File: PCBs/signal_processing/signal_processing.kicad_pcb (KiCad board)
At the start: 2 copper layers, 75 x 36 mm, 140 parts, among them IC1 AD8066, IC2 ADG701BRTZN, IC3 AD8066, IC4 AD8066, IC5 LT1713, IC6 LT1713, IC7 AD8066, X1 87437-0443, X2 87437-0443, X3 87437-0443

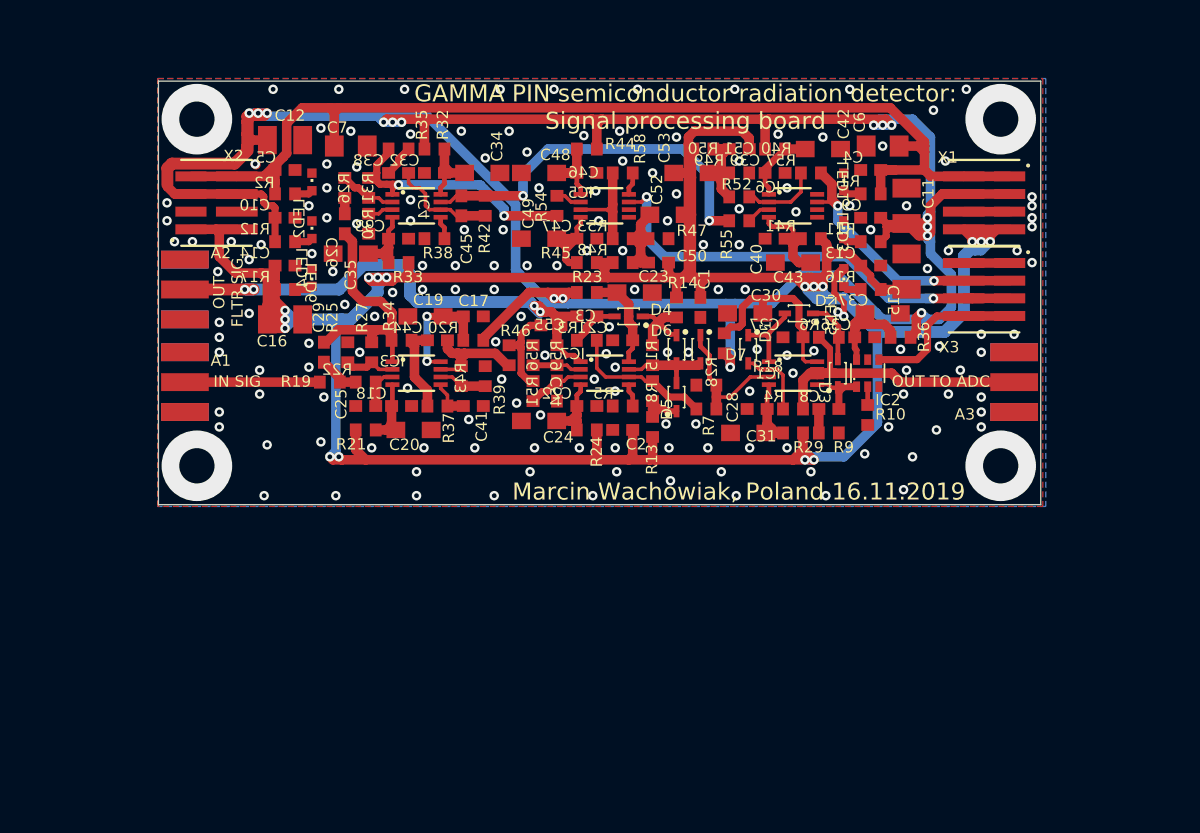
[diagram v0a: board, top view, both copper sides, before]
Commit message: Reorganization of pcb files
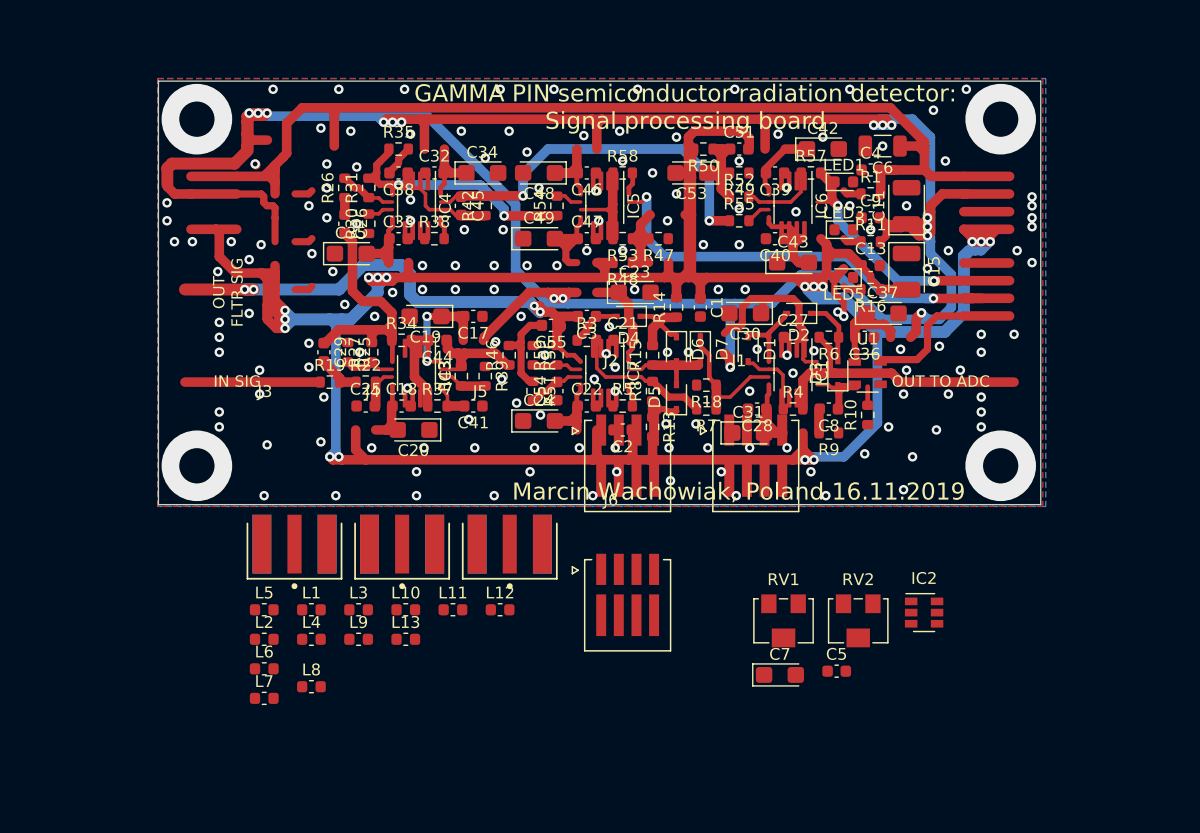
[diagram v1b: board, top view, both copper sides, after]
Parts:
- removed A1, A2, A3: SMA-EDGE-0.062, signal_processing:CONSMA003.062
- removed C10, C14, C50: 100n/50V, signal_processing:C0603
- removed C12, C16: 47u/6V, signal_processing:SMC_B
- removed C52: 4,7u/6V, signal_processing:SMC_A
- removed LED2, LED4, LED6: GREEN, signal_processing:CHIPLED_0603
- removed R12, R17: 300, signal_processing:R0603
- removed R2: 43k, signal_processing:R0603
- removed R20, R21, R23, R24, R28, R29, R32, R33, R36, R40, R41, R44, R45: 1, signal_processing:R0603
- removed X1, X2, X3: 87437-0443, signal_processing:87437-0443
- added IC2: ADG701BRTZN, Package_TO_SOT_SMD:SOT-23-6, F.Cu at (176.1, 132.2)
- added J1: 874380443, semiconductor_radiation_detector:87438-0443, F.Cu at (161.8, 119.7)
- added J2: 874380443, semiconductor_radiation_detector:87438-0443, F.Cu at (150.9, 119.7)
- added J3: CON-SMA-EDGE-S, semiconductor_radiation_detector:CON-SMA-EDGE-S, F.Cu at (122.6, 119.1)
- added J4: CON-SMA-EDGE-S, semiconductor_radiation_detector:CON-SMA-EDGE-S, F.Cu at (131.7, 119.1)
- added J5: CON-SMA-EDGE-S, semiconductor_radiation_detector:CON-SMA-EDGE-S, F.Cu at (140.9, 119.1)
- added J6: 874380443, semiconductor_radiation_detector:87438-0443, F.Cu at (150.9, 131.6)
- added L1: 1u, Inductor_SMD:L_0603_1608Metric, F.Cu at (124.0, 131.9)
- added L10: 1u, Inductor_SMD:L_0603_1608Metric, F.Cu at (132.0, 131.9)
- added L11: 1u, Inductor_SMD:L_0603_1608Metric, F.Cu at (136.0, 131.9)
- added L12: 1u, Inductor_SMD:L_0603_1608Metric, F.Cu at (140.0, 131.9)
- added L13: 1u, Inductor_SMD:L_0603_1608Metric, F.Cu at (132.0, 134.5)
- added L2: 1u, Inductor_SMD:L_0603_1608Metric, F.Cu at (120.0, 134.5)
- added L3: 1u, Inductor_SMD:L_0603_1608Metric, F.Cu at (128.0, 131.9)
- added L4: 1u, Inductor_SMD:L_0603_1608Metric, F.Cu at (124.0, 134.5)
- added L5: 1u, Inductor_SMD:L_0603_1608Metric, F.Cu at (120.0, 131.9)
- added L6: 1u, Inductor_SMD:L_0603_1608Metric, F.Cu at (120.0, 137.0)
- added L7: 1u, Inductor_SMD:L_0603_1608Metric, F.Cu at (120.0, 139.5)
- added L8: 1u, Inductor_SMD:L_0603_1608Metric, F.Cu at (124.0, 138.5)
- added L9: 1u, Inductor_SMD:L_0603_1608Metric, F.Cu at (128.0, 134.5)
- added RV1: 500, Potentiometer_SMD:Potentiometer_Bourns_3224W_Vertical, F.Cu at (164.1, 132.9)
- added RV2: 10, Potentiometer_SMD:Potentiometer_Bourns_3224W_Vertical, F.Cu at (170.5, 132.9)
- C1, C13, C17, C18, C2, C21, C22, C25, C26, C27, C28, C29, C3, C32, C33, C36, C38, C39, C4, C40, C41, C44, C45, C46, C47, C51, C54, C55, C8, C9: footprint signal_processing:C0603 -> Capacitor_SMD:C_0603_1608Metric
- C11, C15: footprint signal_processing:SMC_B -> Capacitor_Tantalum_SMD:CP_EIA-3528-21_Kemet-B
- C19, C20, C23, C24, C30, C31, C34, C35, C37, C42, C43, C48, C49, C53: footprint signal_processing:SMC_A -> Capacitor_Tantalum_SMD:CP_EIA-3216-18_Kemet-A
- C5: value 1n/100V -> 100n/50V; footprint signal_processing:C0603 -> Capacitor_SMD:C_0603_1608Metric
- C6: footprint signal_processing:C1206 -> Capacitor_SMD:C_1206_3216Metric
- C7: value 4,7u/50V -> 4,7u/6V; footprint signal_processing:C1206 -> Capacitor_Tantalum_SMD:CP_EIA-3216-18_Kemet-A
- D1, D2, D3, D4, D5, D6, D7: footprint signal_processing:SOD2514X100N -> Diode_SMD:D_SOD-323
- IC1, IC3, IC4, IC5, IC6, IC7: footprint signal_processing:MSOP8 -> Package_SO:MSOP-8_3x3mm_P0.65mm
- LED1, LED3, LED5: footprint signal_processing:CHIPLED_0603 -> LED_SMD:LED_0603_1608Metric
- R1, R10, R11, R13, R14, R15, R16, R18, R19, R22, R25, R26, R27, R3, R30, R31, R34, R35, R37, R38, R39, R4, R42, R43, R46, R47, R48, R49, R5, R50, R51, R52, R53, R54, R55, R56, R57, R58, R59, R6, R7, R8, R9: footprint signal_processing:R0603 -> Resistor_SMD:R_0603_1608Metric
- U1: renamed from IC2; value ADG701BRTZN -> ADG701; footprint signal_processing:SOT23-6 -> Package_TO_SOT_SMD:SOT-23-6
- moved C5 63.4 mm to (168.7, 137.2), turned to 0 degrees
- moved C7 57.9 mm to (163.8, 137.5)
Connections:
- C5 pad 1: GND -> Net-(C5-Pad1)
- C5 pad 2: /+65V -> -5V
- C7 pad 1: /+65V -> Net-(C5-Pad1)
- C7 pad 2: GND -> -5V
- IC1 pad 1: Net-(D1-PadK) -> Net-(D1-Pad1)
- IC1 pad 2: Net-(D1-PadA) -> Net-(D1-Pad2)
- IC6 pad 7: /RISING_SLOPE -> Net-(IC6-Pad7)
- IC6 pad 8: (no net) -> /RISING_SLOPE
- IC7 pad 7: Net-(D5-PadA) -> Net-(D5-Pad2)
- R1 pad 1: Net-(LED1-PadA) -> /+65V
- R1 pad 2: /+65V -> Net-(LED1-Pad2)
- R10 pad 1: GND -> Net-(R10-Pad1)
- R10 pad 2: Net-(IC2-Pad2) -> GND
- R11 pad 1: Net-(LED3-PadA) -> +5V
- R11 pad 2: +5V -> Net-(LED3-Pad2)
- R13 pad 1: Net-(D5-PadK) -> -5V
- R13 pad 2: -5V -> Net-(D5-Pad1)
- R14 pad 1: Net-(D4-PadK) -> -5V
- R14 pad 2: -5V -> Net-(D4-Pad1)
- R15 pad 1: Net-(D5-PadA) -> Net-(D4-Pad1)
- R15 pad 2: Net-(D4-PadK) -> Net-(D5-Pad2)
- R16 pad 1: -5V -> Net-(LED5-Pad1)
- R16 pad 2: Net-(LED5-PadC) -> -5V
- R18 pad 1: /BLR_OUT -> GND
- R18 pad 2: GND -> /BLR_OUT
- R19 pad 1: /SIGNAL_INPUT -> Net-(C29-Pad2)
- R19 pad 2: Net-(C29-Pad2) -> /SIGNAL_INPUT
- R22 pad 1: Net-(C29-Pad2) -> Net-(C25-Pad2)
- R22 pad 2: Net-(C25-Pad2) -> Net-(C29-Pad2)
- R25 pad 1: GND -> Net-(IC3-Pad2)
- R25 pad 2: Net-(IC3-Pad2) -> GND
- R27 pad 1: Net-(IC3-Pad2) -> /FAST_FILTERED_SIG
- R27 pad 2: /FAST_FILTERED_SIG -> Net-(IC3-Pad2)
- R3 pad 1: Net-(C3-Pad1) -> Net-(IC7-Pad6)
- R3 pad 2: Net-(IC7-Pad6) -> Net-(C3-Pad1)
- R30 pad 1: GND -> Net-(IC4-Pad3)
- R30 pad 2: Net-(IC4-Pad3) -> GND
- R31 pad 1: Net-(IC4-Pad2) -> Net-(IC4-Pad1)
- R31 pad 2: Net-(IC4-Pad1) -> Net-(IC4-Pad2)
- R34 pad 1: /FAST_FILTERED_SIG -> Net-(C44-Pad2)
- R34 pad 2: Net-(C44-Pad2) -> /FAST_FILTERED_SIG
- R35 pad 1: Net-(IC4-Pad1) -> Net-(C38-Pad2)
- R35 pad 2: Net-(C38-Pad2) -> Net-(IC4-Pad1)
- R37 pad 1: Net-(C44-Pad2) -> Net-(C41-Pad2)
- R37 pad 2: Net-(C41-Pad2) -> Net-(C44-Pad2)
- R38 pad 1: GND -> Net-(IC4-Pad5)
- R38 pad 2: Net-(IC4-Pad5) -> GND
- R39 pad 1: GND -> Net-(IC3-Pad6)
- R39 pad 2: Net-(IC3-Pad6) -> GND
- R4 pad 1: Net-(D1-PadA) -> /ADC
- R4 pad 2: /ADC -> Net-(D1-Pad2)
- R42 pad 1: Net-(C38-Pad1) -> Net-(C45-Pad1)
- R42 pad 2: Net-(C45-Pad1) -> Net-(C38-Pad1)
- R43 pad 1: Net-(IC3-Pad6) -> Net-(C44-Pad1)
- R43 pad 2: Net-(C44-Pad1) -> Net-(IC3-Pad6)
- R46 pad 1: Net-(C44-Pad1) -> Net-(C55-Pad2)
- R46 pad 2: Net-(C55-Pad2) -> Net-(C44-Pad1)
- R47 pad 1: GND -> Net-(R47-Pad1)
- R47 pad 2: Net-(C50-Pad1) -> GND
- R48 pad 1: Net-(C50-Pad1) -> -5V
- R48 pad 2: -5V -> Net-(R48-Pad2)
- R49 pad 1: GND -> Net-(R49-Pad1)
- R49 pad 2: Net-(C51-Pad1) -> GND
- R5 pad 1: GND -> Net-(IC7-Pad5)
- R5 pad 2: Net-(IC7-Pad5) -> GND
- R50 pad 1: Net-(C51-Pad1) -> -5V
- R50 pad 2: -5V -> Net-(R50-Pad2)
- R51 pad 1: Net-(C55-Pad2) -> Net-(C54-Pad2)
- R51 pad 2: Net-(C54-Pad2) -> Net-(C55-Pad2)
- R52 pad 1: Net-(C51-Pad1) -> Net-(IC6-Pad2)
- R52 pad 2: Net-(IC6-Pad2) -> Net-(C51-Pad1)
- R53 pad 1: Net-(C50-Pad1) -> Net-(IC5-Pad3)
- R53 pad 2: Net-(IC5-Pad3) -> Net-(C5-Pad1)
- R54 pad 1: Net-(IC4-Pad1) -> Net-(IC5-Pad2)
- R54 pad 2: Net-(IC5-Pad2) -> Net-(IC4-Pad1)
- R55 pad 1: Net-(C45-Pad1) -> Net-(IC6-Pad3)
- R55 pad 2: Net-(IC6-Pad3) -> Net-(C45-Pad1)
- R56 pad 1: GND -> Net-(IC7-Pad2)
- R56 pad 2: Net-(IC7-Pad2) -> GND
- R57 pad 1: Net-(IC6-Pad2) -> Net-(IC6-Pad7)
- R57 pad 2: /RISING_SLOPE -> Net-(IC6-Pad2)
- R58 pad 1: Net-(IC5-Pad3) -> Net-(IC5-Pad8)
- R58 pad 2: Net-(IC5-Pad8) -> Net-(IC5-Pad3)
- R59 pad 1: Net-(IC7-Pad2) -> /FILTERED_SIGNAL
- R59 pad 2: /FILTERED_SIGNAL -> Net-(IC7-Pad2)
- R6 pad 1: Net-(D2-PadK) -> /ADC
- R6 pad 2: /ADC -> Net-(D2-Pad1)
- R7 pad 1: /BLR_OUT -> Net-(IC7-Pad6)
- R7 pad 2: Net-(IC7-Pad6) -> /BLR_OUT
- R8 pad 1: Net-(D5-PadK) -> Net-(IC7-Pad6)
- R8 pad 2: Net-(IC7-Pad6) -> Net-(D5-Pad1)
- R9 pad 1: GND -> Net-(C8-Pad2)
- R9 pad 2: Net-(C8-Pad2) -> GND
- U1 pad 2: Net-(IC2-Pad2) -> Net-(R10-Pad1)
- U1 pad 3: GND -> (no net)
- U1 pad 6: Net-(C36-Pad2) -> (no net)
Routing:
- net /RESET: track 13.8 -> 0.00 mm
- net (no net): track 0.00 -> 13.8 mm
- net Net-(C29-Pad2): track 3.93 -> 15.4 mm
- net /SIGNAL_INPUT: track 11.5 -> 0.00 mm
- net GND: track 12.7 -> 20.4 mm, vias 167 -> 162
- net Net-(D1-PadK): track 6.76 -> 0.00 mm
- net Net-(D1-Pad1): track 0.00 -> 6.76 mm
- net Net-(IC4-Pad1): track 24.2 -> 26.4 mm
- net Net-(IC5-Pad2): track 2.23 -> 0.00 mm
- net Net-(IC4-Pad3): track 2.16 -> 0.00 mm
- net Net-(IC6-Pad3): track 2.06 -> 0.00 mm, vias 0 -> 1
- net Net-(C45-Pad1): track 32.2 -> 34.3 mm
- net Net-(IC5-Pad3): track 9.03 -> 11.0 mm
- net Net-(IC7-Pad5): track 1.95 -> 0.00 mm
- net Net-(IC5-Pad8): track 1.95 -> 0.00 mm
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
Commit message: finished preamplifier board redesigning
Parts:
- removed the IC1 at (164.9, 111.8)
- removed the IC7 at (148.9, 111.8)
- added IC2: AD8066, Package_SO:MSOP-8_3x3mm_P0.65mm, F.Cu at (140.1, 141.9)
- added IC3: AD8066, Package_SO:MSOP-8_3x3mm_P0.65mm, F.Cu at (140.1, 146.4)
- added R44: 1k, Resistor_SMD:R_0603_1608Metric, F.Cu at (153.2, 140.8)
- added R45: 2k, Resistor_SMD:R_0603_1608Metric, F.Cu at (153.2, 143.3)
- added R46: 1k, Resistor_SMD:R_0603_1608Metric, F.Cu at (153.2, 145.9)
- added R47: 2k, Resistor_SMD:R_0603_1608Metric, F.Cu at (153.2, 148.4)
- IC5: renamed from IC2; value ADG701BRTZN -> ADG701
- moved IC6 51.8 mm to (147.5, 146.4), turned to 0 degrees
- moved J2 51.3 mm to (104.8, 97.2), turned to 270 degrees
- moved J6 48.5 mm to (191.5, 105.2), turned to 90 degrees
- moved IC4 46.6 mm to (147.5, 141.9), turned to 0 degrees
- moved J1 35.6 mm to (189.4, 97.3), turned to 90 degrees
- renumbered C15 to C10, C17 to C11, C18 to C12, C19 to C13, C20 to C14, C21 to C15, C22 to C16, C23 to C17, C24 to C18, C26 to C19, C25 to C20, C29 to C21, C27 to C22, C28 to C23, C30 to C24, C31 to C25, C32 to C26, C33 to C27, C34 to C28, C35 to C29, C36 to C30, C37 to C31, C38 to C32, C39 to C33, C40 to C34, C41 to C35, C42 to C36, C43 to C37, C44 to C38, C45 to C39, C46 to C40, C47 to C41, C48 to C42, C49 to C43, C51 to C44, C5 to C45, C53 to C46, C7 to C47, C54 to C48, C55 to C49, C6 to C5, C8 to C6, C9 to C7, C11 to C8, C13 to C9, IC3 to IC1, IC5 to IC7, LED3 to LED2, LED5 to LED3, R3 to R1, R13 to R10, R14 to R12, R15 to R13, R18 to R14, R16 to R15, R19 to R16, R22 to R17, R25 to R18, R26 to R19, R4 to R2, R27 to R20, R30 to R21, R31 to R22, R34 to R23, R35 to R24, R37 to R25, R38 to R26, R39 to R27, R42 to R28, R43 to R29, R5 to R3, R49 to R30, R50 to R31, R46 to R32, R47 to R33, R48 to R34, R51 to R35, R52 to R36, R55 to R37, R53 to R38, R54 to R39, R1 to R4, R56 to R40, R57 to R41, R58 to R42, R59 to R43, R6 to R5, R7 to R6, R8 to R7, R9 to R8, R10 to R9
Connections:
- C20 pad 2: Net-(C25-Pad2) -> Net-(C20-Pad2)
- C32 pad 1: Net-(C38-Pad1) -> Net-(C32-Pad1)
- C35 pad 2: Net-(C41-Pad2) -> Net-(C35-Pad2)
- C38 pad 1: Net-(C44-Pad1) (its old number) -> Net-(C38-Pad1)
- C39 pad 1: Net-(C45-Pad1) (its old number) -> Net-(C39-Pad1)
- C39 pad 2: Net-(C38-Pad1) -> Net-(C32-Pad1)
- C48 pad 2: Net-(C54-Pad2) -> Net-(C48-Pad2)
- IC1 pad 1: /FAST_FILTERED_SIG -> Net-(D1-Pad1)
- IC1 pad 2: Net-(IC3-Pad2) -> Net-(D1-Pad2)
- IC1 pad 3: Net-(C25-Pad2) -> /BLR_OUT
- IC1 pad 5: Net-(C41-Pad2) -> Net-(IC1-Pad5)
- IC1 pad 6: Net-(IC3-Pad6) -> Net-(IC1-Pad6)
- IC1 pad 7: Net-(C44-Pad1) (its old number) -> Net-(D5-Pad2)
- IC4 pad 1: Net-(IC4-Pad1) -> /FILTERED_SIGNAL
- IC4 pad 3: Net-(IC4-Pad3) -> Net-(C48-Pad2)
- IC4 pad 5: Net-(IC4-Pad5) -> Net-(C35-Pad2)
- IC4 pad 6: Net-(C38-Pad1) -> Net-(IC4-Pad6)
- IC4 pad 7: Net-(C45-Pad1) (its old number) -> Net-(C38-Pad1)
- IC6 pad 8: /RISING_SLOPE -> Net-(IC6-Pad8)
- IC7 pad 7: /PULSE_DURATION -> Net-(IC7-Pad7)
- R1 pad 1: Net-(IC7-Pad6) -> Net-(IC1-Pad6)
- R17 pad 1: Net-(C25-Pad2) -> Net-(C20-Pad2)
- R18 pad 1: Net-(IC3-Pad2) -> Net-(IC2-Pad2)
- R19 pad 2: Net-(IC4-Pad2) -> Net-(IC3-Pad2)
- R20 pad 2: Net-(IC3-Pad2) -> Net-(IC2-Pad2)
- R21 pad 1: Net-(IC4-Pad3) -> Net-(IC3-Pad3)
- R22 pad 1: Net-(IC4-Pad1) -> Net-(IC3-Pad1)
- R22 pad 2: Net-(IC4-Pad2) -> Net-(IC3-Pad2)
- R24 pad 2: Net-(IC4-Pad1) -> Net-(IC3-Pad1)
- R25 pad 1: Net-(C41-Pad2) -> Net-(C35-Pad2)
- R26 pad 1: Net-(IC4-Pad5) -> Net-(IC3-Pad5)
- R27 pad 1: Net-(IC3-Pad6) -> Net-(IC4-Pad6)
- R28 pad 1: Net-(C45-Pad1) (its old number) -> Net-(C39-Pad1)
- R28 pad 2: Net-(C38-Pad1) -> Net-(C32-Pad1)
- R29 pad 1: Net-(C44-Pad1) (its old number) -> Net-(C38-Pad1)
- R29 pad 2: Net-(IC3-Pad6) -> Net-(IC4-Pad6)
- R3 pad 1: Net-(IC7-Pad5) -> Net-(IC1-Pad5)
- R32 pad 2: Net-(C44-Pad1) (its old number) -> Net-(C38-Pad1)
- R35 pad 1: Net-(C54-Pad2) -> Net-(C48-Pad2)
- R37 pad 2: Net-(C45-Pad1) (its old number) -> Net-(C39-Pad1)
- R39 pad 2: Net-(IC4-Pad1) -> Net-(IC3-Pad1)
- R40 pad 1: Net-(IC7-Pad2) (its old number) -> Net-(IC4-Pad2)
- R43 pad 2: Net-(IC7-Pad2) (its old number) -> Net-(IC4-Pad2)
- R6 pad 1: Net-(IC7-Pad6) -> Net-(IC1-Pad6)
- R7 pad 1: Net-(IC7-Pad6) -> Net-(IC1-Pad6)
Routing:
- net Net-(C45-Pad1) (its old number): track 34.3 -> 0.00 mm, vias 2 -> 0
- net Net-(C45-Pad1): track 0.00 -> 32.2 mm, vias 0 -> 2
- net Net-(C44-Pad1) (its old number): track 11.3 -> 0.00 mm
- net Net-(C51-Pad1): track 0.00 -> 11.3 mm
- net Net-(IC7-Pad3): track 11.0 -> 1.95 mm
- net Net-(IC5-Pad3): track 0.00 -> 9.03 mm
- net Net-(C36-Pad2): track 0.00 -> 8.67 mm
- net Net-(C30-Pad2): track 8.67 -> 0.00 mm
- net Net-(C55-Pad2): track 0.00 -> 8.13 mm
- net Net-(C49-Pad2): track 8.13 -> 0.00 mm
- net Net-(C44-Pad2): track 0.00 -> 8.04 mm
- net Net-(C8-Pad1): track 0.00 -> 6.35 mm
- net Net-(C6-Pad1): track 6.35 -> 0.00 mm
- net Net-(C38-Pad2): track 8.04 -> 2.74 mm
- net Net-(IC7-Pad2) (its old number): track 4.19 -> 0.00 mm, vias 1 -> 0
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
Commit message: sp board update
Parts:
- removed the C19 at (126.8, 99.1)
- removed the C22 at (164.9, 108.8)
- removed the C23 at (161.9, 114.9)
- removed the C24 at (160.9, 106.7)
- removed the C28 at (138.5, 94.8)
- removed the C33 at (163.4, 94.8)
- removed the C34 at (163.4, 100.4)
- removed the C36 at (167.5, 92.8)
- removed the C37 at (164.9, 102.4)
- removed the C39 at (136.7, 97.6)
- removed the C43 at (143.4, 100.4)
- removed the C44 at (160.4, 92.8)
- removed the C47 at (163.8, 137.5)
- removed the IC5 at (176.1, 132.2)
- removed the J3 at (122.6, 119.1)
- removed the L11 at (136.0, 131.9)
- removed the R19 at (126.8, 96.1)
- removed the R22 at (128.9, 96.1)
- removed the R30 at (160.4, 94.8)
- removed the R31 at (157.3, 92.8)
- removed the R33 at (153.5, 100.4)
- removed the R36 at (160.4, 96.8)
- removed the R46 at (153.2, 145.9)
- removed the R47 at (153.2, 148.4)
- added C11: 100n/50V, Capacitor_SMD:C_0603_1608Metric, F.Cu at (136.1, 98.0)
- added C12: 4,7u/6V, Capacitor_Tantalum_SMD:CP_EIA-3216-18_Kemet-A, F.Cu at (130.8, 96.2)
- added C14: 4,7u/6V, Capacitor_Tantalum_SMD:CP_EIA-3216-18_Kemet-A, F.Cu at (164.8, 108.8)
- added C15: 100n/50V, Capacitor_SMD:C_0603_1608Metric, F.Cu at (152.1, 97.4)
- added C16: 4,7u/6V, Capacitor_Tantalum_SMD:CP_EIA-3216-18_Kemet-A, F.Cu at (152.9, 95.6)
- added C17: 100n/50V, Capacitor_SMD:C_0603_1608Metric, F.Cu at (140.7, 97.3)
- added C18: 4,7u/6V, Capacitor_Tantalum_SMD:CP_EIA-3216-18_Kemet-A, F.Cu at (138.8, 96.5)
- added C20: 4,7u/6V, Capacitor_Tantalum_SMD:CP_EIA-3216-18_Kemet-A, F.Cu at (168.4, 110.9)
- added C26: 4,7u/6V, Capacitor_Tantalum_SMD:CP_EIA-3216-18_Kemet-A, F.Cu at (127.8, 105.0)
- added C29: 100n/50V, Capacitor_SMD:C_0603_1608Metric, F.Cu at (157.9, 100.2)
- added C30: 4,7u/6V, Capacitor_Tantalum_SMD:CP_EIA-3216-18_Kemet-A, F.Cu at (159.7, 99.3)
- added C48: 100n/50V, Capacitor_SMD:C_0603_1608Metric, F.Cu at (141.4, 95.1)
- added C49: 4,7u/6V, Capacitor_Tantalum_SMD:CP_EIA-3216-18_Kemet-A, F.Cu at (144.0, 95.0)
- added C50: 1p/50V, Capacitor_SMD:C_0603_1608Metric, F.Cu at (126.9, 97.0)
- added J1: CON-SMA-EDGE-S, semiconductor_radiation_detector:CON-SMA-EDGE-S, F.Cu at (106.3, 112.6)
- added L3: 1u, Inductor_SMD:L_0603_1608Metric, F.Cu at (134.7, 96.5)
- added R18: 1k, Resistor_SMD:R_0603_1608Metric, F.Cu at (157.5, 102.5)
- added R25: 100k, Resistor_SMD:R_0603_1608Metric, F.Cu at (155.1, 97.4)
- added R29: 100, Resistor_SMD:R_0603_1608Metric, F.Cu at (149.8, 98.9)
- added R35: 1, Resistor_SMD:R_0603_1608Metric, F.Cu at (130.0, 98.0)
- added R43: 22k, Resistor_SMD:R_0603_1608Metric, F.Cu at (144.4, 98.1)
- added R44: 2k, Resistor_SMD:R_0603_1608Metric, F.Cu at (147.5, 101.2)
- added R45: 2,2k, Resistor_SMD:R_0603_1608Metric, F.Cu at (141.4, 93.5)
- added R8: 560, Resistor_SMD:R_0603_1608Metric, F.Cu at (137.9, 109.3)
- C25, C31: value 4,7u/6V -> 100n/50V; footprint Capacitor_Tantalum_SMD:CP_EIA-3216-18_Kemet-A -> Capacitor_SMD:C_0603_1608Metric
- C32: value 470p/50V -> 4,7u/6V; footprint Capacitor_SMD:C_0603_1608Metric -> Capacitor_Tantalum_SMD:CP_EIA-3216-18_Kemet-A
- C33: renamed from C21; value 200p/50V -> 2,2n/50V
- C34: renamed from C38; value 180p/50V -> 2,2n/50V
- C35: renamed from C49; value 160p/50V -> 2,2n/50V
- C36: renamed from C20; value 200p/50V -> 2,2n/50V
- C37: renamed from C35; value 180p/50V -> 2,2n/50V
- C38: renamed from C48; value 160p/50V -> 220p/50V
- C45: value 100n/50V -> 1p/50V
- C46: value 4,7u/6V -> 470p/50V; footprint Capacitor_Tantalum_SMD:CP_EIA-3216-18_Kemet-A -> Capacitor_SMD:C_0603_1608Metric
- R10: renamed from R20; value 9,1k -> 820
- R11: renamed from R29; value 8,2k -> 1k
- R12: renamed from R43; value 6,8k -> 680
- R13: renamed from R18; value 1,8k -> 270
- R14: renamed from R27; value 2k -> 270
- R15: renamed from R40; value 3,3k -> 470
- R21, R26: value 100 -> 1k
- R24: value 1 -> 520
- R28: value 470k -> 1
- R32: value 6,2k -> 100
- R34: value 1 -> 470k
- R38: value 520 -> 100
- R39: value 100 -> 3,3k
- R4: renamed from R16; value 3k -> 390
- R41: value 22k -> 1k
- R42: value 100k -> 1k
- R5: renamed from R17; value 33k -> 2,4k
- R6: renamed from R23; value 3,6k -> 330
- R7: renamed from R25; value 30k -> 3,3k
- RV1: value 500 -> 10
- RV2: value 10 -> 500
- moved L4 54.7 mm to (164.0, 107.0), turned to 180 degrees
- moved J6 50.3 mm to (190.8, 112.5), turned to 270 degrees
- moved L5 49.9 mm to (152.1, 93.7), turned to 180 degrees
- moved C45 49.3 mm to (135.7, 100.5), turned to 270 degrees
- moved R33 48.3 mm to (156.0, 95.1), turned to 90 degrees
- moved IC6 46.9 mm to (153.8, 99.9)
- moved IC3 46.6 mm to (131.7, 100.6)
- moved L6 44.6 mm to (137.0, 95.8), turned to 270 degrees
- moved L7 44.3 mm to (167.7, 114.7), turned to 90 degrees
- moved RV2 44.3 mm to (147.8, 94.8)
- moved R30 43.9 mm to (157.9, 97.2), turned to 90 degrees
- moved L11 41.0 mm to (158.4, 116.1)
- moved L12 34.9 mm to (159.8, 103.2), turned to 270 degrees
- moved C25 34.1 mm to (130.0, 103.1)
- moved L13 33.5 mm to (144.1, 103.2)
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- renumbered C4 to C1, C17 to C10, C26 to C13, C30 to C19, C5 to C2, C12 to C21, C14 to C22, C16 to C23, C18 to C24, C29 to C28, C7 to C3, C3 to C39, C8 to C4, C1 to C43, C2 to C44, C6 to C47, C9 to C5, C10 to C6, C11 to C7, C13 to C8, C15 to C9, D7 to D1, D5 to D2, D6 to D3, D1 to D5, D2 to D6, D3 to D7, U1 to IC5, J1 to J2, J2 to J3, J6 to J4, J4 to J5, J5 to J6, L8 to L11, L3 to L2, L7 to L4, L9 to L7, L2 to L8, L4 to L9, LED3 to LED1, LED1 to LED2, LED2 to LED3, R4 to R1, R6 to R16, R1 to R17, R13 to R19, R11 to R2, R14 to R20, R3 to R22, R7 to R23, R10 to R27, R15 to R3, R44 to R30, R12 to R31, R45 to R33, R2 to R36, R5 to R40, R8 to R46, R9 to R47, R35 to R9
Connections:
- C19 pad 2: Net-(C30-Pad2) -> Net-(C19-Pad2)
- C25 pad 1: GND -> Net-(C25-Pad1)
- C25 pad 2: Net-(C23-Pad1) (its old number) -> GND
- C31 pad 1: Net-(C30-Pad2) -> Net-(C31-Pad1)
- C32 pad 1: Net-(C32-Pad1) -> GND
- C32 pad 2: Net-(C32-Pad2) -> Net-(C31-Pad1)
- C34 pad 1: Net-(C38-Pad1) -> Net-(C34-Pad1)
- C35 pad 2: Net-(C49-Pad2) -> Net-(C35-Pad2)
- C36 pad 2: Net-(C20-Pad2) -> Net-(C36-Pad2)
- C37 pad 2: Net-(C35-Pad2) -> Net-(C37-Pad2)
- C38 pad 2: Net-(C48-Pad2) -> Net-(C38-Pad2)
- C40 pad 1: GND -> Net-(C40-Pad1)
- C40 pad 2: Net-(C40-Pad2) -> /FAST_FILTERED_SIG
- C41 pad 2: GND -> -5V
- C42 pad 1: Net-(C40-Pad2) -> Net-(C41-Pad1)
- C42 pad 2: GND -> -5V
- C45 pad 2: -5V -> Net-(C45-Pad2)
- C46 pad 1: Net-(C44-Pad1) -> Net-(C45-Pad2)
- C46 pad 2: -5V -> Net-(C46-Pad2)
- C47 pad 1: Net-(C6-Pad1) -> Net-(C47-Pad1)
- D1 pad 2: Net-(D5-Pad2) -> Net-(D1-Pad2)
- D2 pad 2: Net-(D5-Pad2) -> Net-(D1-Pad2)
- D3 pad 2: Net-(D5-Pad2) -> Net-(D1-Pad2)
- D5 pad 1: Net-(D1-Pad1) -> Net-(D5-Pad1)
- D5 pad 2: Net-(D1-Pad2) -> Net-(D5-Pad2)
- D6 pad 2: Net-(D1-Pad1) -> Net-(D5-Pad1)
- D7 pad 1: Net-(C6-Pad1) -> Net-(C47-Pad1)
- IC1 pad 1: Net-(D1-Pad1) -> /FAST_FILTERED_SIG
- IC1 pad 2: Net-(D1-Pad2) -> Net-(IC1-Pad2)
- IC1 pad 3: /BLR_OUT -> Net-(C36-Pad2)
- IC1 pad 5: Net-(IC1-Pad5) -> Net-(C37-Pad2)
- IC1 pad 7: Net-(D5-Pad2) -> Net-(C34-Pad1)
- IC2 pad 1: /FAST_FILTERED_SIG -> /FILTERED_SIGNAL
- IC2 pad 3: Net-(C20-Pad2) -> Net-(C38-Pad2)
- IC2 pad 5: Net-(C6-Pad1) -> Net-(IC2-Pad5)
- IC2 pad 6: /ADC -> Net-(IC2-Pad6)
- IC2 pad 7: /ADC -> Net-(D1-Pad2)
- IC3 pad 1: Net-(IC3-Pad1) -> Net-(C50-Pad1)
- IC3 pad 2: Net-(IC3-Pad2) -> Net-(C50-Pad2)
- IC3 pad 4: Net-(C23-Pad1) (its old number) -> Net-(C25-Pad1)
- IC3 pad 6: Net-(C32-Pad1) -> Net-(C45-Pad2)
- IC3 pad 7: Net-(C39-Pad1) (its old number) -> Net-(C45-Pad1)
- IC3 pad 8: Net-(C22-Pad2) -> Net-(C11-Pad2)
- IC4 pad 1: /FILTERED_SIGNAL -> Net-(D5-Pad1)
- IC4 pad 2: Net-(IC4-Pad2) -> Net-(D5-Pad2)
- IC4 pad 3: Net-(C48-Pad2) -> /BLR_OUT
- IC4 pad 5: Net-(C35-Pad2) -> Net-(C47-Pad1)
- IC4 pad 6: Net-(IC4-Pad6) -> /ADC
- IC4 pad 7: Net-(C38-Pad1) -> /ADC
- IC5 pad 1: Net-(C6-Pad1) -> Net-(C47-Pad1)
- IC5 pad 3: (no net) -> GND
- IC5 pad 6: (no net) -> Net-(C19-Pad2)
- IC6 pad 1: Net-(C33-Pad2) (its old number) -> Net-(C15-Pad2)
- IC6 pad 4: Net-(C34-Pad1) -> Net-(C29-Pad1)
- IC7 pad 1: Net-(C40-Pad2) -> Net-(C17-Pad2)
- IC7 pad 4: Net-(C41-Pad1) -> Net-(C31-Pad1)
- L10 pad 1: +5V -> Net-(C25-Pad1)
- L10 pad 2: Net-(C33-Pad2) (its old number) -> -5V
- L12 pad 1: +5V -> Net-(C29-Pad1)
- L12 pad 2: Net-(C40-Pad2) -> -5V
- L13 pad 1: Net-(C41-Pad1) -> Net-(C31-Pad1)
- L5 pad 2: Net-(C22-Pad2) -> Net-(C15-Pad2)
- L6 pad 1: Net-(C23-Pad1) (its old number) -> +5V
- L6 pad 2: -5V -> Net-(C17-Pad2)
- L7 pad 2: Net-(C30-Pad2) -> Net-(C19-Pad2)
- R10 pad 2: Net-(IC2-Pad2) -> Net-(IC1-Pad2)
- R11 pad 1: Net-(C38-Pad1) -> Net-(C34-Pad1)
- R11 pad 2: Net-(IC4-Pad6) -> Net-(IC1-Pad6)
- R12 pad 2: Net-(IC4-Pad2) -> Net-(IC2-Pad2)
- R13 pad 1: Net-(IC2-Pad2) -> Net-(IC1-Pad2)
- R14 pad 1: Net-(IC4-Pad6) -> Net-(IC1-Pad6)
- R15 pad 1: Net-(IC4-Pad2) -> Net-(IC2-Pad2)
- R16 pad 1: Net-(IC1-Pad6) -> Net-(IC2-Pad6)
- R17 pad 1: Net-(IC1-Pad6) -> Net-(IC2-Pad6)
- R19 pad 2: Net-(D5-Pad2) -> Net-(D1-Pad2)
- R21 pad 1: Net-(IC3-Pad3) -> Net-(C50-Pad1)
- R21 pad 2: GND -> Net-(C50-Pad2)
- R22 pad 1: Net-(IC1-Pad5) -> Net-(IC2-Pad5)
- R23 pad 1: Net-(IC1-Pad6) -> Net-(IC2-Pad6)
- R24 pad 1: Net-(C32-Pad2) -> Net-(IC6-Pad3)
- R24 pad 2: Net-(IC3-Pad1) -> Net-(C41-Pad1)
- R26 pad 1: Net-(IC3-Pad5) -> Net-(C40-Pad1)
- R26 pad 2: GND -> Net-(C50-Pad2)
- R28 pad 1: Net-(C39-Pad1) (its old number) -> -5V
- R28 pad 2: Net-(C32-Pad1) -> Net-(R28-Pad2)
- R30 pad 1: Net-(IC7-Pad7) -> Net-(IC6-Pad7)
- R32 pad 1: Net-(C49-Pad2) -> Net-(IC3-Pad3)
- R32 pad 2: Net-(C38-Pad1) -> GND
- R34 pad 1: -5V -> Net-(C45-Pad1)
- R34 pad 2: Net-(R34-Pad2) -> Net-(C45-Pad2)
- R36 pad 2: Net-(D1-Pad2) -> Net-(D5-Pad2)
- R37 pad 1: Net-(IC6-Pad3) -> Net-(IC7-Pad3)
- R37 pad 2: Net-(C39-Pad1) (its old number) -> Net-(C45-Pad1)
- R38 pad 1: Net-(IC7-Pad3) -> Net-(IC3-Pad5)
- R38 pad 2: Net-(C45-Pad1) -> GND
- R39 pad 1: Net-(IC7-Pad2) -> Net-(R39-Pad1)
- R39 pad 2: Net-(IC3-Pad1) -> GND
- R41 pad 1: Net-(IC6-Pad7) -> Net-(IC7-Pad8)
- R41 pad 2: Net-(IC6-Pad2) -> /RISING_SLOPE
- R42 pad 1: Net-(IC7-Pad8) -> Net-(IC7-Pad2)
- R42 pad 2: Net-(IC7-Pad3) -> Net-(C48-Pad1)
- R5 pad 1: Net-(C20-Pad2) -> Net-(C36-Pad2)
- R7 pad 1: Net-(C35-Pad2) -> Net-(C37-Pad2)
- R9 pad 1: Net-(C48-Pad2) -> Net-(C38-Pad2)
- R9 pad 2: Net-(C49-Pad2) -> Net-(C35-Pad2)
- RV1 pad 2: Net-(C44-Pad1) -> Net-(C41-Pad1)
- RV1 pad 3: Net-(R31-Pad2) -> Net-(R28-Pad2)
- RV2 pad 1: Net-(R33-Pad1) -> Net-(R39-Pad1)
- RV2 pad 2: Net-(C45-Pad1) -> Net-(C48-Pad1)
- RV2 pad 3: Net-(R34-Pad2) -> Net-(R45-Pad2)
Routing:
- net -5V: track 278.2 -> 3.00 mm, vias 17 -> 0
- net +5V: track 244.2 -> 1.54 mm, vias 18 -> 0
- net /+65V: track 97.3 -> 1.54 mm
- net /FILTERED_SIGNAL: track 46.6 -> 5.29 mm, vias 4 -> 0
- net /PULSE_DURATION: track 41.2 -> 1.94 mm, vias 2 -> 0
- net Net-(C45-Pad1): track 32.2 -> 5.17 mm, vias 2 -> 0
- net Net-(IC4-Pad1): track 24.2 -> 0.00 mm, vias 2 -> 0
- net /RISING_SLOPE: track 22.8 -> 1.52 mm, vias 2 -> 0
- net GND: track 20.4 -> 0.00 mm, vias 160 -> 0
- net Net-(C22-Pad2): track 17.9 -> 0.00 mm
- net Net-(C50-Pad1): track 12.6 -> 28.7 mm, vias 0 -> 2
- net /FAST_FILTERED_SIG: track 23.2 -> 8.11 mm
- net /ADC: track 25.9 -> 11.2 mm, vias 0 -> 1
- net Net-(D1-Pad2): track 0.00 -> 14.3 mm
- net (no net): track 13.8 -> 0.00 mm
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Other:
- board text added: "FILTERED SIGNAL"
- board text added: "Semiconductor radiation detector: signal processing board, Marcin Wachowiak, Poland"
- board text removed: "GAMMA PIN semiconductor radiation detector: Signal processing board"
- board text removed: "Marcin Wachowiak, Poland 16.11.2019"
- board text removed: "OUT AMPL /FLTR SIG"
- board text removed: "OUT FLTR SIG"

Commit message: finished pcbs
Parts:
- moved J4 7.38 mm to (174.8, 104.2)
- moved J2 7.38 mm to (174.8, 96.8)
- moved J6 7.37 mm to (183.4, 112.6)
- moved C1 7.37 mm to (164.8, 96.6)
- moved C2 7.37 mm to (166.6, 93.9)
- moved C3 7.37 mm to (164.8, 99.6)
- moved C4 7.37 mm to (167.2, 97.6)
- moved C5 7.37 mm to (164.8, 102.6)
- moved C6 7.37 mm to (167.2, 102.6)
- moved LED1 7.37 mm to (161.7, 102.6)
- moved LED2 7.37 mm to (161.7, 96.6)
- moved LED3 7.37 mm to (161.7, 99.6)
- moved R1 7.37 mm to (163.3, 96.6)
- moved R2 7.37 mm to (163.3, 99.6)
- moved R3 7.37 mm to (163.3, 102.6)
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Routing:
- net -5V: track 3.00 -> 297.3 mm, vias 0 -> 21
- net +5V: track 1.54 -> 250.0 mm, vias 0 -> 17
- net /+65V: track 1.54 -> 76.6 mm
- net GND: track 0.00 -> 63.8 mm, vias 0 -> 83
- net /RISING_SLOPE: track 1.52 -> 33.8 mm, vias 0 -> 2
- net /FILTERED_SIGNAL: track 5.29 -> 35.2 mm, vias 0 -> 2
- net /PULSE_DURATION: track 1.94 -> 31.0 mm, vias 0 -> 2
- net /RESET: track 0.00 -> 16.9 mm
- net /ADC: track 11.2 -> 25.0 mm, vias 1 -> 2
- net /SIGNAL_INPUT: track 0.00 -> 8.55 mm
- net /FAST_FILTERED_SIG: track 8.11 -> 14.3 mm
- net Net-(C19-Pad2): track 1.69 -> 5.63 mm
- net Net-(IC5-Pad2): track 1.15 -> 3.59 mm
- net Net-(C13-Pad2): track 9.93 -> 12.0 mm
- net Net-(D1-Pad2): track 14.3 -> 15.5 mm
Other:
- board size 75 x 36 mm -> 63.1 x 36 mm
- board text added: "FLTR SIG"
- board text removed: "FILTERED SIGNAL"
